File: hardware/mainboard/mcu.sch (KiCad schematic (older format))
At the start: 20 parts, among them J2 Tag-Connect SWD, J3 USB_MICRO_RIGHT, SW1 RESET, U7 ATSAMD21G18A-AUT, U8 MCP4728

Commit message: Fix a few more mpns
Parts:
- C19, C20, C21, C22, C49, C50: mpn alt GRM188R72A104KA35D -> GCM188R91E104KA37D
- C23: mpn (none) -> GRM21BR61E106KA73K; mpn alt GRM21BR61E106KA73K -> (none)
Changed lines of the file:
@@
 F 5 "MF-CAP-0603-0.1uF" H 3150 7000 50  0001 C CNN "mpn"
 F 6 "10%, 25v" H 3150 7000 50  0001 C CNN "mpn specs"
-F 7 "GRM188R72A104KA35D" H 3150 7000 50  0001 C CNN "mpn alt"
+F 7 "GCM188R91E104KA37D" H 3150 7000 50  0001 C CNN "mpn alt"
 	1    3150 7000
 	1    0    0    -1
@@
 F 5 "MF-CAP-0603-0.1uF" H 3650 7000 50  0001 C CNN "mpn"
 F 6 "10%, 25v" H 3650 7000 50  0001 C CNN "mpn specs"
-F 7 "GRM188R72A104KA35D" H 3650 7000 50  0001 C CNN "mpn alt"
+F 7 "GCM188R91E104KA37D" H 3650 7000 50  0001 C CNN "mpn alt"
 	1    3650 7000
 	1    0    0    -1
@@
 F 5 "MF-CAP-0603-0.1uF" H 4150 7000 50  0001 C CNN "mpn"
 F 6 "10%, 25v" H 4150 7000 50  0001 C CNN "mpn specs"
-F 7 "GRM188R72A104KA35D" H 4150 7000 50  0001 C CNN "mpn alt"
+F 7 "GCM188R91E104KA37D" H 4150 7000 50  0001 C CNN "mpn alt"
 	1    4150 7000
 	1    0    0    -1
@@
 F 5 "MF-CAP-0603-0.1uF" H 7750 5900 50  0001 C CNN "mpn"
 F 6 "10%, 25v" H 7750 5900 50  0001 C CNN "mpn specs"
-F 7 "GRM188R72A104KA35D" H 7750 5900 50  0001 C CNN "mpn alt"
+F 7 "GCM188R91E104KA37D" H 7750 5900 50  0001 C CNN "mpn alt"
 	1    7750 5900
 	1    0    0    -1
@@
 F 3 "~" H 8300 5900 50  0001 C CNN
 F 4 "yes" H 8300 5900 50  0001 C CNN "finalized"
-F 5 "" H 8300 5900 50  0001 C CNN "mpn"
+F 5 "GRM21BR61E106KA73K" H 8300 5900 50  0001 C CNN "mpn"
 F 6 "10% 16v" H 8300 5900 50  0001 C CNN "mpn specs"
-F 7 "GRM21BR61E106KA73K" H 8300 5900 50  0001 C CNN "mpn alt"
+F 7 "" H 8300 5900 50  0001 C CNN "mpn alt"
 	1    8300 5900
 	1    0    0    -1
@@
 F 5 "MF-CAP-0603-0.1uF" H 2700 7000 50  0001 C CNN "mpn"
 F 6 "10%, 25v" H 2700 7000 50  0001 C CNN "mpn specs"
-F 7 "GRM188R72A104KA35D" H 2700 7000 50  0001 C CNN "mpn alt"
+F 7 "GCM188R91E104KA37D" H 2700 7000 50  0001 C CNN "mpn alt"
 	1    2700 7000
 	1    0    0    -1
@@
 F 5 "MF-CAP-0603-0.1uF" H 2250 7000 50  0001 C CNN "mpn"
 F 6 "10%, 25v" H 2250 7000 50  0001 C CNN "mpn specs"
-F 7 "GRM188R72A104KA35D" H 2250 7000 50  0001 C CNN "mpn alt"
+F 7 "GCM188R91E104KA37D" H 2250 7000 50  0001 C CNN "mpn alt"
 	1    2250 7000
 	1    0    0    -1

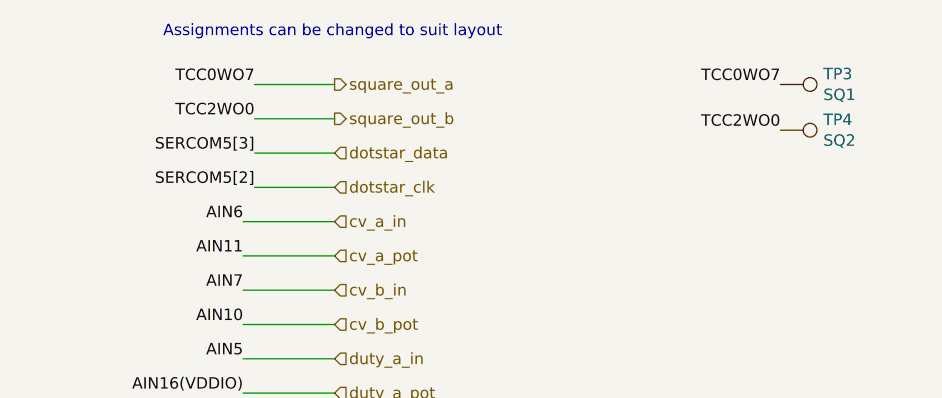
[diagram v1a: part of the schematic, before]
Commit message: Move Pollux's square generator to TCC1WO1
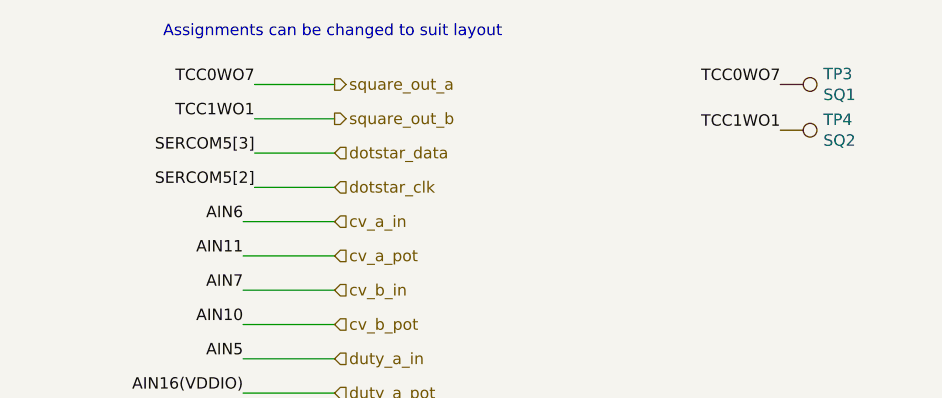
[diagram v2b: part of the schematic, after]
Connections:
- net TCC1WO1 is gone; now on net square_out_b: U7.16 (PA11)
- net square_out_b: no longer U7.25 (PA16)
- new net TCC2WO0: U7.25 (PA16)
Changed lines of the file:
@@
 	1    0    0    -1
 $EndComp
-Text Label 5550 1150 2    50   ~ 0
-TCC2WO0
 Wire Wire Line
 	5550 1000 5900 1000
@@
 	0    1    1    0
 $EndComp
-Text Label 7850 1200 2    50   ~ 0
-TCC2WO0
 Text Label 3850 2850 0    50   ~ 0
 SERCOM5[2]
@@
 	0    1    1    0
 $EndComp
+Text Label 5550 1150 2    50   ~ 0
+TCC1WO1
+Text Label 7850 1200 2    50   ~ 0
+TCC1WO1
 $EndSCHEMATC

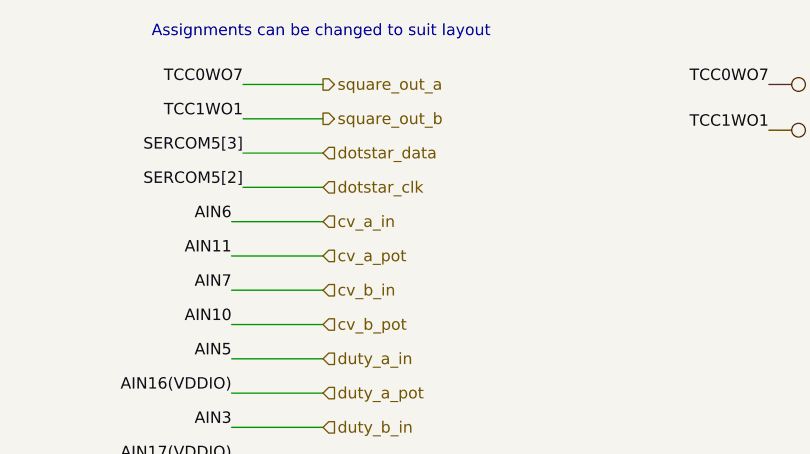
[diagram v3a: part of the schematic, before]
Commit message: Swap dotstar clk and data on mainboard (label only change, no hardware change)
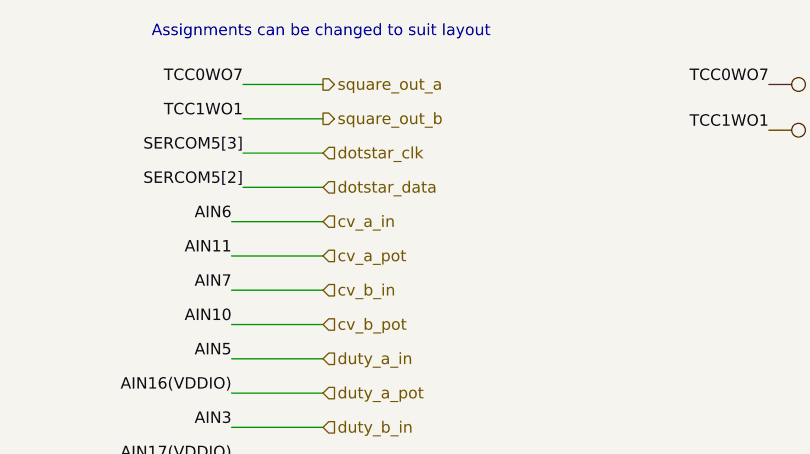
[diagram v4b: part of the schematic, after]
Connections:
- net dotstar_clk: now also U7.38 (PB23); no longer U7.37 (PB22)
- net dotstar_data: now also U7.37 (PB22); no longer U7.38 (PB23)
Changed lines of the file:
@@
 Text HLabel 5900 1150 2    50   Output ~ 0
 square_out_b
+Text HLabel 5900 1450 2    50   Input ~ 0
+dotstar_data
 Text HLabel 5900 1300 2    50   Input ~ 0
-dotstar_data
-Text HLabel 5900 1450 2    50   Input ~ 0
 dotstar_clk
 Text HLabel 5900 1600 2    50   Input ~ 0

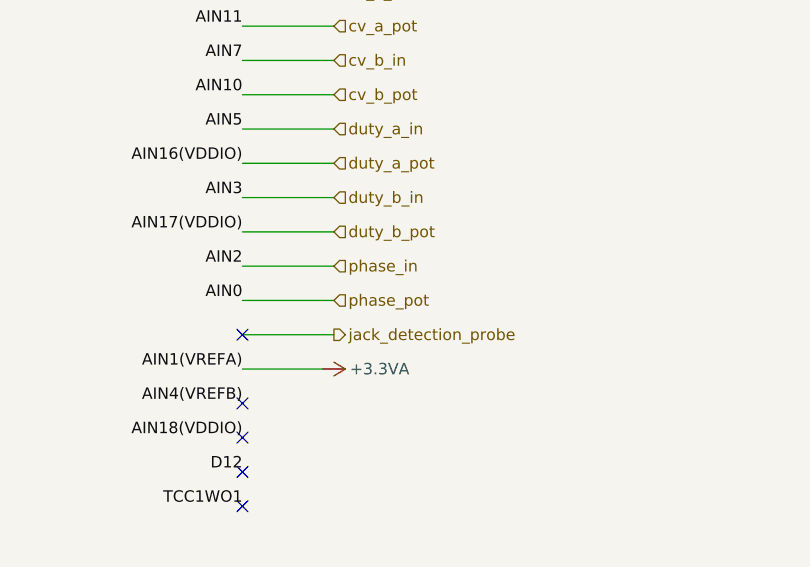
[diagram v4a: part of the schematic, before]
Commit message: Change phase in to hard sync button, remove unneeded parts, make v2 mainboard
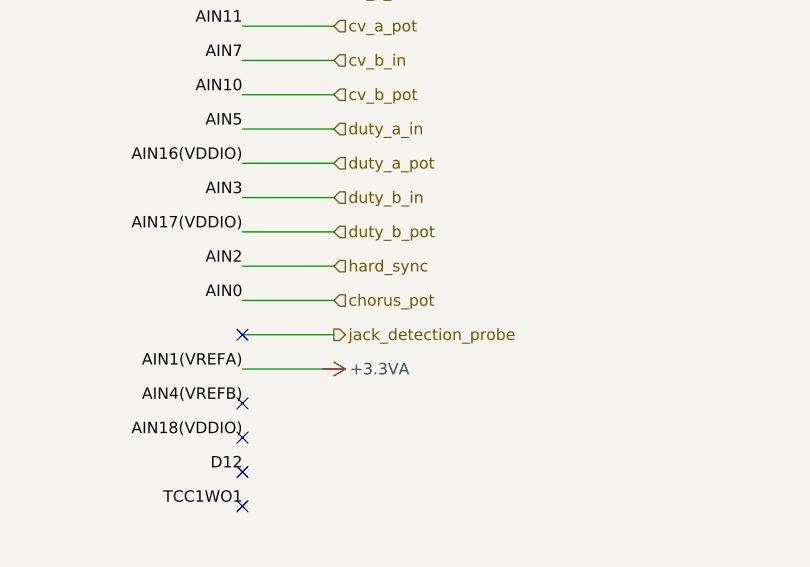
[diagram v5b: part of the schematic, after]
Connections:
- net phase_in renamed hard_sync
- net phase_pot renamed chorus_pot
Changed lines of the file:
@@
 Sheet 6 7
 Title "Castor & Pollux"
-Date "2020-09-07"
-Rev "v1"
+Date "2020-09-26"
+Rev "v2"
 Comp "Winterbloom"
 Comment1 "CC BY-SA 4.0"
@@
 duty_b_in
 Text HLabel 5900 2800 2    50   Input ~ 0
-phase_in
+hard_sync
 Text HLabel 5900 2950 2    50   Input ~ 0
-phase_pot
+chorus_pot
 Text HLabel 5900 3100 2    50   Output ~ 0
 jack_detection_probe

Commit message: Update mpns
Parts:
- J3: footprint MF_Connectors:MF_Connectors-MICROUSB-RIGHT -> mainboard:MF_Connectors-MICROUSB-RIGHT
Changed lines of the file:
@@
 F 0 "J3" H 9572 5842 45  0000 R CNN
 F 1 "USB_MICRO_RIGHT" H 9572 5758 45  0000 R CNN
-F 2 "MF_Connectors:MF_Connectors-MICROUSB-RIGHT" V 9568 5704 20  0001 C CNN
+F 2 "mainboard:MF_Connectors-MICROUSB-RIGHT" V 9568 5704 20  0001 C CNN
 F 3 "" H 9791 5850 60  0000 C CNN
 F 4 "yes" H 9800 5850 50  0001 C CNN "finalized"

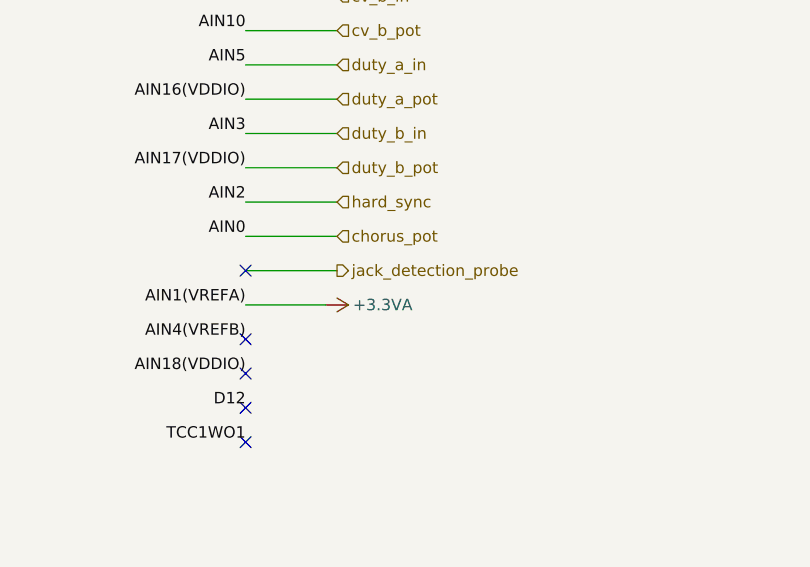
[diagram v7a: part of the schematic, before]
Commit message: Cleanup some comments in the schematic
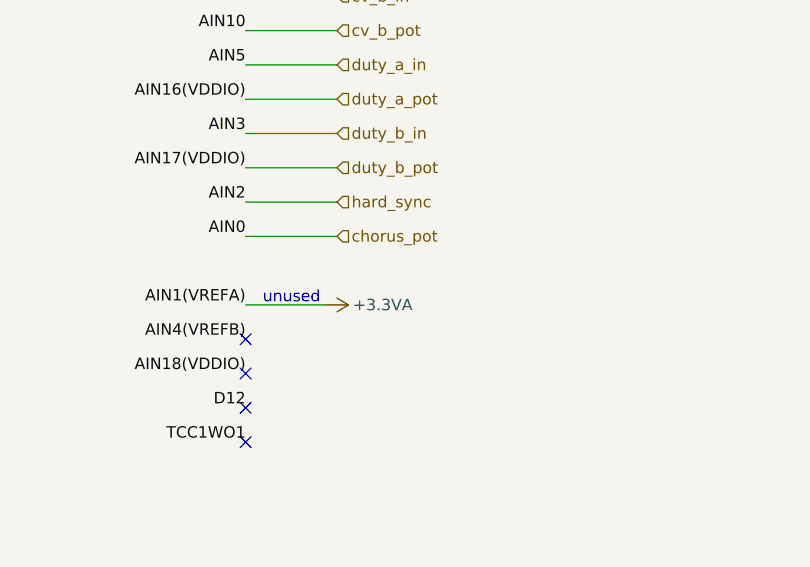
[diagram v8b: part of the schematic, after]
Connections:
- no-connect marks 22 -> 21
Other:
- note added: "unused"
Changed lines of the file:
@@
 Text HLabel 5900 2950 2    50   Input ~ 0
 chorus_pot
-Text HLabel 5900 3100 2    50   Output ~ 0
-jack_detection_probe
 Text Label 1850 2450 2    50   ~ 0
 AIN0
@@
 Wire Wire Line
 	5500 2950 5900 2950
-Wire Wire Line
-	5900 3100 5500 3100
 Text Label 5500 2800 2    50   ~ 0
 AIN2
@@
 AIN4(VREFB)
 NoConn ~ 5500 3400
-NoConn ~ 5500 3100
 NoConn ~ 1850 3450
 NoConn ~ 1850 3550
@@
 Text Label 7850 1200 2    50   ~ 0
 TCC1WO1
+Text Notes 5575 3250 0    50   ~ 0
+unused
 $EndSCHEMATC
